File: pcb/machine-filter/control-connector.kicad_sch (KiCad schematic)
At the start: 3 parts

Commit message: Control chips placed; board-to-board connectors found by search: 4 lines (22+3+5+3 pins, 12 ground)
connector_search.py: lines live in legal straight runs on both boards (courtyard polygons, socket body and its
courtyard, leads under bodies), d's ground rules plus a ground on every connector; simulated annealing, 12
restarts. sync_headers.py deletes and re-adds the header footprints from the schematic, places both boards and
checks every pin pair lines up. auto_place.py now keeps other parts' leads out from under a body (U6 had RV4's
lead under it). Mux channels and LED sections re-checked: already shortest. Build OK, raw DRC: no real problems.

Co-Authored-By: Claude Opus 5.5 <noreply@anthropic.com>
Claude-Session: https://claude.ai/code/session_01Cf5qNBi3oNHhbCjPHvswth
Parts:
- added JA4: 1x3 socket, Connector_PinSocket_2.54mm:PinSocket_1x03_P2.54mm_Vertical, symbol Connector_Generic:Conn_01x03
- JA1: value 1x15 socket -> 1x22 socket; footprint Connector_PinSocket_2.54mm:PinSocket_1x15_P2.54mm_Vertical -> Connector_PinSocket_2.54mm:PinSocket_1x22_P2.54mm_Vertical; symbol Connector_Generic:Conn_01x15 -> Connector_Generic:Conn_01x22; MPN 2.54 mm female header 1x15, 8.5 mm (as the Seed3 sockets) -> 2.54 mm female header 1x22, 8.5 mm (as the Seed3 sockets)
- JA2: value 1x13 socket -> 1x3 socket; footprint Connector_PinSocket_2.54mm:PinSocket_1x13_P2.54mm_Vertical -> Connector_PinSocket_2.54mm:PinSocket_1x03_P2.54mm_Vertical; symbol Connector_Generic:Conn_01x13 -> Connector_Generic:Conn_01x03; MPN 2.54 mm female header 1x13, 8.5 mm (as the Seed3 sockets) -> 2.54 mm female header 1x3, 8.5 mm (as the Seed3 sockets)
- JA3: value 1x10 socket -> 1x5 socket; footprint Connector_PinSocket_2.54mm:PinSocket_1x10_P2.54mm_Vertical -> Connector_PinSocket_2.54mm:PinSocket_1x05_P2.54mm_Vertical; symbol Connector_Generic:Conn_01x10 -> Connector_Generic:Conn_01x05; MPN 2.54 mm female header 1x10, 8.5 mm (as the Seed3 sockets) -> 2.54 mm female header 1x5, 8.5 mm (as the Seed3 sockets)
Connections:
- net CTL_+12V: now also JA1.13 (Pin_13); no longer JA1.12 (Pin_12)
- net CTL_+3V3_A: now also JA1.8 (Pin_8); no longer JA3.9 (Pin_9)
- net CTL_-12V: now also JA1.18 (Pin_18); no longer JA1.14 (Pin_14)
- net CTL_CV_BASE: now also JA1.10 (Pin_10); no longer JA2.2 (Pin_2)
- net CTL_CV_DIST: now also JA4.1 (Pin_1); no longer JA2.12 (Pin_12)
- net CTL_CV_EQF: now also JA1.21 (Pin_21); no longer JA2.9 (Pin_9)
- net CTL_CV_EQG: now also JA2.3 (Pin_3); no longer JA2.8 (Pin_8)
- net CTL_CV_HPRES: now also JA1.20 (Pin_20); no longer JA2.5 (Pin_5)
- net CTL_CV_LPRES: now also JA2.1 (Pin_1); no longer JA2.6 (Pin_6)
- net CTL_CV_SRR: now also JA4.3 (Pin_3); no longer JA2.11 (Pin_11)
- net CTL_CV_WIDTH: now also JA1.11 (Pin_11); no longer JA2.3 (Pin_3)
- net CTL_GND: now also JA1.12 (Pin_12), JA1.14 (Pin_14), JA1.17 (Pin_17), JA1.19 (Pin_19), JA1.22 (Pin_22), JA2.2 (Pin_2), JA3.5 (Pin_5), JA4.2 (Pin_2); no longer JA1.11 (Pin_11), JA1.13 (Pin_13), JA1.15 (Pin_15), JA2.1 (Pin_1), JA2.10 (Pin_10), JA2.13 (Pin_13), JA2.4 (Pin_4), JA2.7 (Pin_7), JA3.1 (Pin_1), JA3.10 (Pin_10), JA3.3 (Pin_3), JA3.6 (Pin_6), JA3.8 (Pin_8)
- net CTL_IN_L: now also JA1.6 (Pin_6); no longer JA1.2 (Pin_2)
- net CTL_IN_R: now also JA1.5 (Pin_5); no longer JA1.3 (Pin_3)
- net CTL_LED_A: now also JA3.1 (Pin_1); no longer JA1.10 (Pin_10)
- net CTL_MUX_A: now also JA3.4 (Pin_4); no longer JA3.7 (Pin_7)
- net CTL_MUX_B: now also JA3.2 (Pin_2); no longer JA3.5 (Pin_5)
- net CTL_MUX_C: now also JA3.3 (Pin_3); no longer JA3.4 (Pin_4)
- net CTL_OUT_L: now also JA1.3 (Pin_3); no longer JA1.6 (Pin_6)
- net CTL_OUT_R: now also JA1.2 (Pin_2); no longer JA1.5 (Pin_5)
- net CTL_POT_MUX: now also JA1.16 (Pin_16); no longer JA3.2 (Pin_2)
- net CTL_POT_VOL: now also JA1.15 (Pin_15); no longer JA1.8 (Pin_8)
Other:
- note added: "4 single-row 2.54 mm headers: JA* female on the control board's back, JB* male on the main board's front"
- note added: "JA1: pin 1 at (44.45, 25.4) mm,"
- note added: "JA2: pin 1 at (67.31, 59.69) mm,"
- note added: "JA3: pin 1 at (26.67, 68.58) mm,"
- note added: "JA4: pin 1 at (57.15, 111.76) mm,"
- note removed: "3 single-row 2.54 mm headers: JA* female on the control board's back, JB* male on the main board's front"
- note removed: "JA1: pin 1 at (21.95, 69.205) mm,"
- note removed: "JA2: pin 1 at (41.635, 66.03) mm,"
- note removed: "JA3: pin 1 at (21.95, 84.445) mm,"

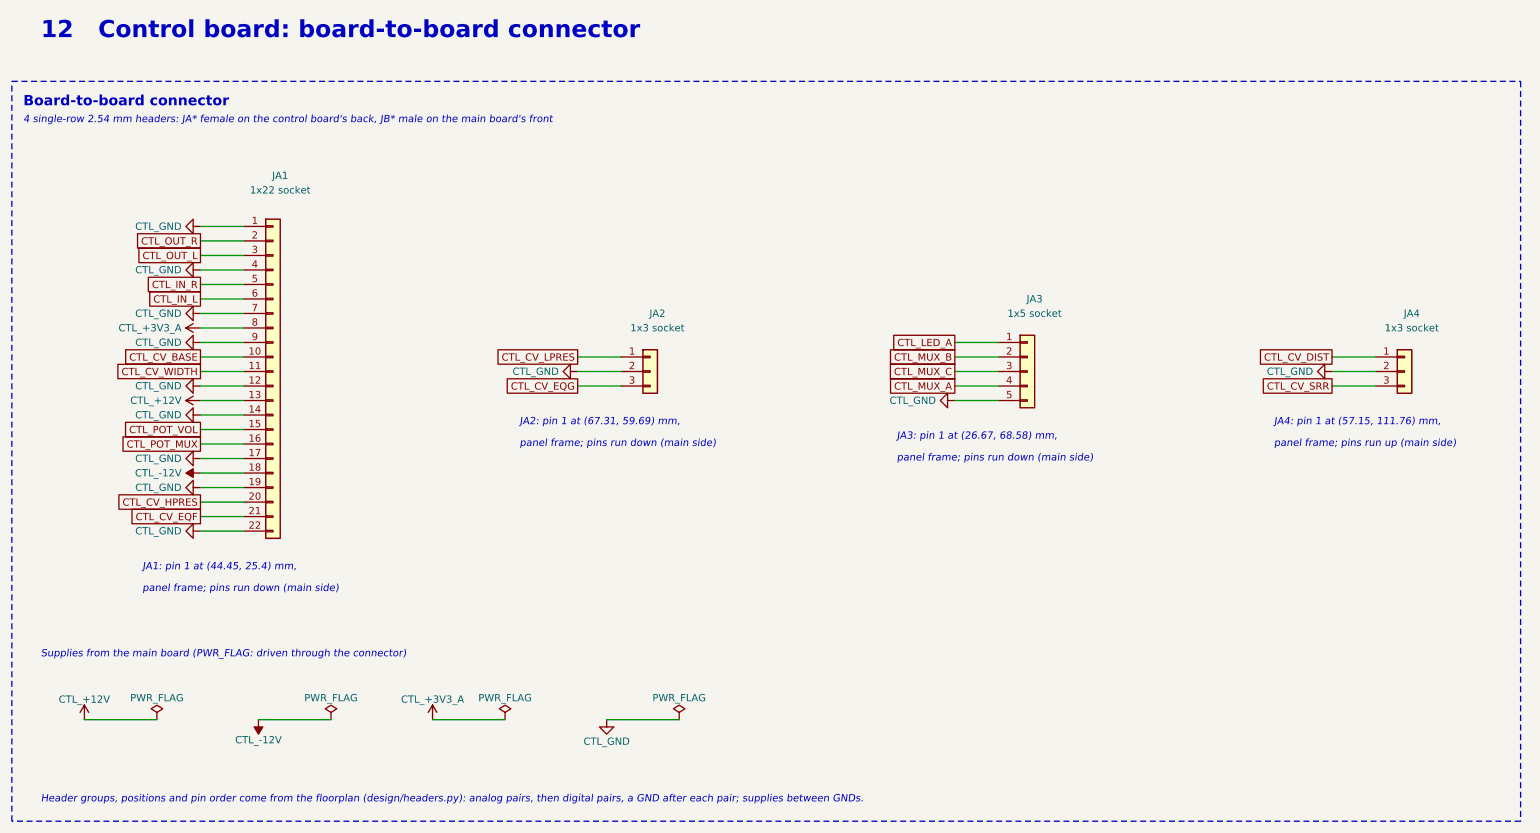
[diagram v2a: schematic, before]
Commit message: Hand-soldering clearance (d: 1.25 mm): connectors re-searched, control parts re-placed
connector_search.py: header pads keep 1.25 mm from every other pad on both boards and from the whole box around
each jack, pot and LED (taken from the square pin-1 pad); --free leaves parts to be re-placed out of the search.
auto_place.py: control-board through-hole pads and anything near a header keep 1.25 mm; --free re-places parts.
Result: 3 lines, 30 + 5 + 2 pins (16 ground); the connector beside pot RV5 and the one between two CV jacks are
gone. Measured: nearest header-pad gap 1.35 mm, header to a body box 1.31 mm. Raw DRC: no real problems.

Co-Authored-By: Claude Opus 5.5 <noreply@anthropic.com>
Claude-Session: https://claude.ai/code/session_01Cf5qNBi3oNHhbCjPHvswth
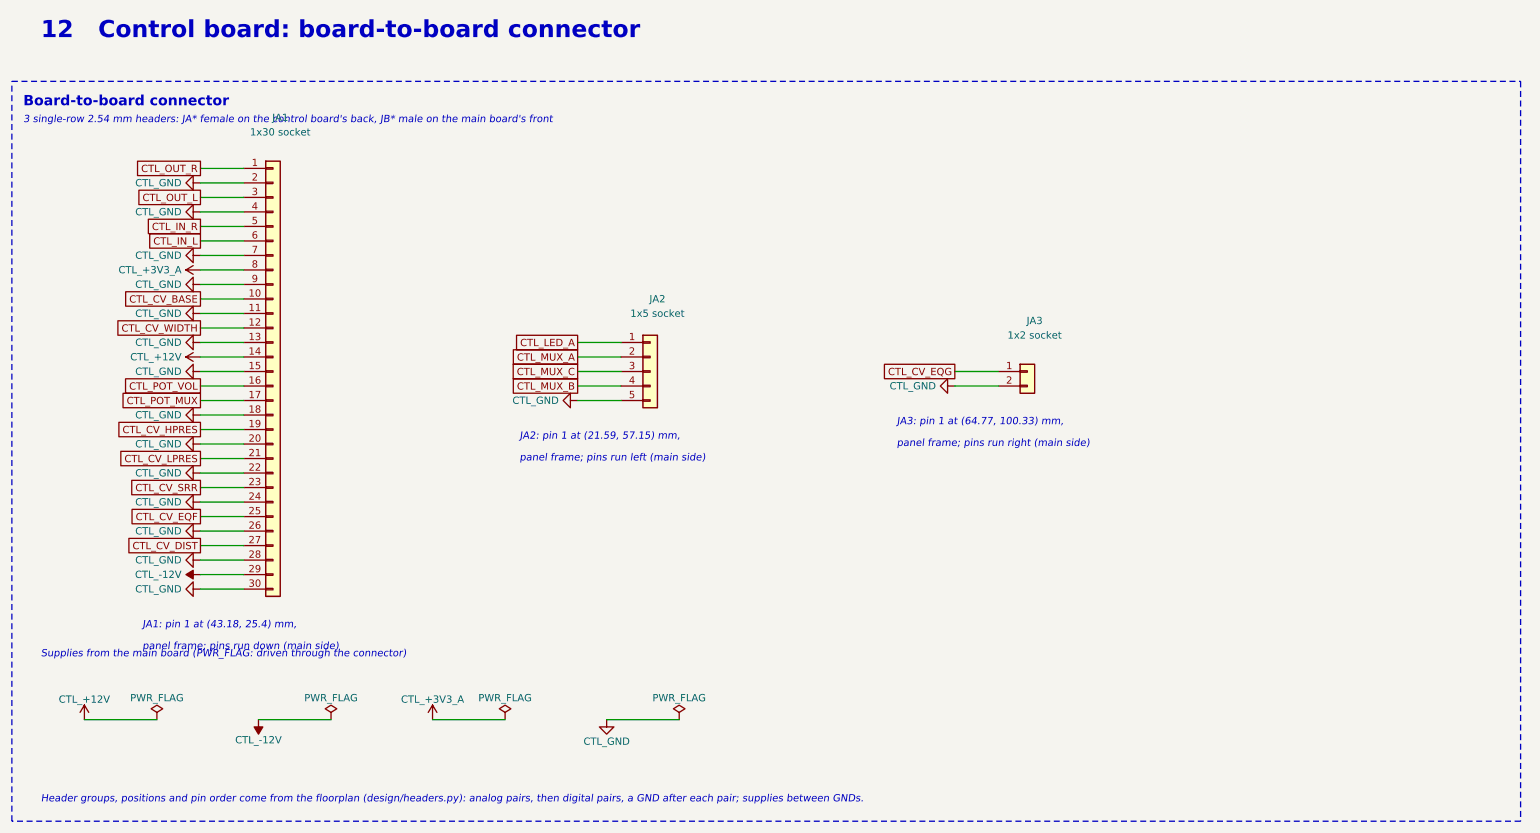
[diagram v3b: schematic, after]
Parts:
- removed JA4: 1x3 socket, Connector_PinSocket_2.54mm:PinSocket_1x03_P2.54mm_Vertical, symbol Connector_Generic:Conn_01x03
- JA1: value 1x22 socket -> 1x30 socket; footprint Connector_PinSocket_2.54mm:PinSocket_1x22_P2.54mm_Vertical -> Connector_PinSocket_2.54mm:PinSocket_1x30_P2.54mm_Vertical; symbol Connector_Generic:Conn_01x22 -> Connector_Generic:Conn_01x30; MPN 2.54 mm female header 1x22, 8.5 mm (as the Seed3 sockets) -> 2.54 mm female header 1x30, 8.5 mm (as the Seed3 sockets)
- JA2: value 1x3 socket -> 1x5 socket; footprint Connector_PinSocket_2.54mm:PinSocket_1x03_P2.54mm_Vertical -> Connector_PinSocket_2.54mm:PinSocket_1x05_P2.54mm_Vertical; symbol Connector_Generic:Conn_01x03 -> Connector_Generic:Conn_01x05; MPN 2.54 mm female header 1x3, 8.5 mm (as the Seed3 sockets) -> 2.54 mm female header 1x5, 8.5 mm (as the Seed3 sockets)
- JA3: value 1x5 socket -> 1x2 socket; footprint Connector_PinSocket_2.54mm:PinSocket_1x05_P2.54mm_Vertical -> Connector_PinSocket_2.54mm:PinSocket_1x02_P2.54mm_Vertical; symbol Connector_Generic:Conn_01x05 -> Connector_Generic:Conn_01x02; MPN 2.54 mm female header 1x5, 8.5 mm (as the Seed3 sockets) -> 2.54 mm female header 1x2, 8.5 mm (as the Seed3 sockets)
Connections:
- net CTL_+12V: now also JA1.14 (Pin_14); no longer JA1.13 (Pin_13)
- net CTL_-12V: now also JA1.29 (Pin_29); no longer JA1.18 (Pin_18)
- net CTL_CV_DIST: now also JA1.27 (Pin_27)
- net CTL_CV_EQF: now also JA1.25 (Pin_25); no longer JA1.21 (Pin_21)
- net CTL_CV_EQG: now also JA3.1 (Pin_1); no longer JA2.3 (Pin_3)
- net CTL_CV_HPRES: now also JA1.19 (Pin_19); no longer JA1.20 (Pin_20)
- net CTL_CV_LPRES: now also JA1.21 (Pin_21); no longer JA2.1 (Pin_1)
- net CTL_CV_SRR: now also JA1.23 (Pin_23)
- net CTL_CV_WIDTH: now also JA1.12 (Pin_12); no longer JA1.11 (Pin_11)
- net CTL_GND: now also JA1.11 (Pin_11), JA1.13 (Pin_13), JA1.15 (Pin_15), JA1.18 (Pin_18), JA1.2 (Pin_2), JA1.20 (Pin_20), JA1.24 (Pin_24), JA1.26 (Pin_26), JA1.28 (Pin_28), JA1.30 (Pin_30), JA2.5 (Pin_5), JA3.2 (Pin_2); no longer JA1.1 (Pin_1), JA1.12 (Pin_12), JA1.14 (Pin_14), JA1.17 (Pin_17), JA1.19 (Pin_19), JA2.2 (Pin_2), JA3.5 (Pin_5)
- net CTL_LED_A: now also JA2.1 (Pin_1); no longer JA3.1 (Pin_1)
- net CTL_MUX_A: now also JA2.2 (Pin_2); no longer JA3.4 (Pin_4)
- net CTL_MUX_B: now also JA2.4 (Pin_4); no longer JA3.2 (Pin_2)
- net CTL_MUX_C: now also JA2.3 (Pin_3); no longer JA3.3 (Pin_3)
- net CTL_OUT_R: now also JA1.1 (Pin_1); no longer JA1.2 (Pin_2)
- net CTL_POT_MUX: now also JA1.17 (Pin_17); no longer JA1.16 (Pin_16)
- net CTL_POT_VOL: now also JA1.16 (Pin_16); no longer JA1.15 (Pin_15)
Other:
- note added: "3 single-row 2.54 mm headers: JA* female on the control board's back, JB* male on the main board's front"
- note added: "JA1: pin 1 at (43.18, 25.4) mm,"
- note added: "JA2: pin 1 at (21.59, 57.15) mm,"
- note added: "JA3: pin 1 at (64.77, 100.33) mm,"
- note added: "panel frame; pins run left (main side)"
- note added: "panel frame; pins run right (main side)"
- note removed: "4 single-row 2.54 mm headers: JA* female on the control board's back, JB* male on the main board's front"
- note removed: "JA1: pin 1 at (44.45, 25.4) mm,"
- note removed: "JA2: pin 1 at (67.31, 59.69) mm,"
- note removed: "JA3: pin 1 at (26.67, 68.58) mm,"
- note removed: "JA4: pin 1 at (57.15, 111.76) mm,"
- note removed: "panel frame; pins run up (main side)"

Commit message: Experiment (not chosen): connectors searched with a strict Seed-pocket rule; routing tool runs
The board now holds the pocket-rule connectors (4 lines, 34 pins) as an experiment; c08-handsolder (3 lines,
routed: main 5 unrouted / 61 vias, control 2 unrouted / 16 vias, DRC 0) stays the best candidate. route_board.py:
Freerouting 2.3 ignores direction costs from DSN, CLI and freerouting.json (tested); 90-degree snap works.
Paused for d: the header loop is repeating (post-mortem 2026-10-06).

Co-Authored-By: Claude Opus 5.5 <noreply@anthropic.com>
Claude-Session: https://claude.ai/code/session_01Cf5qNBi3oNHhbCjPHvswth
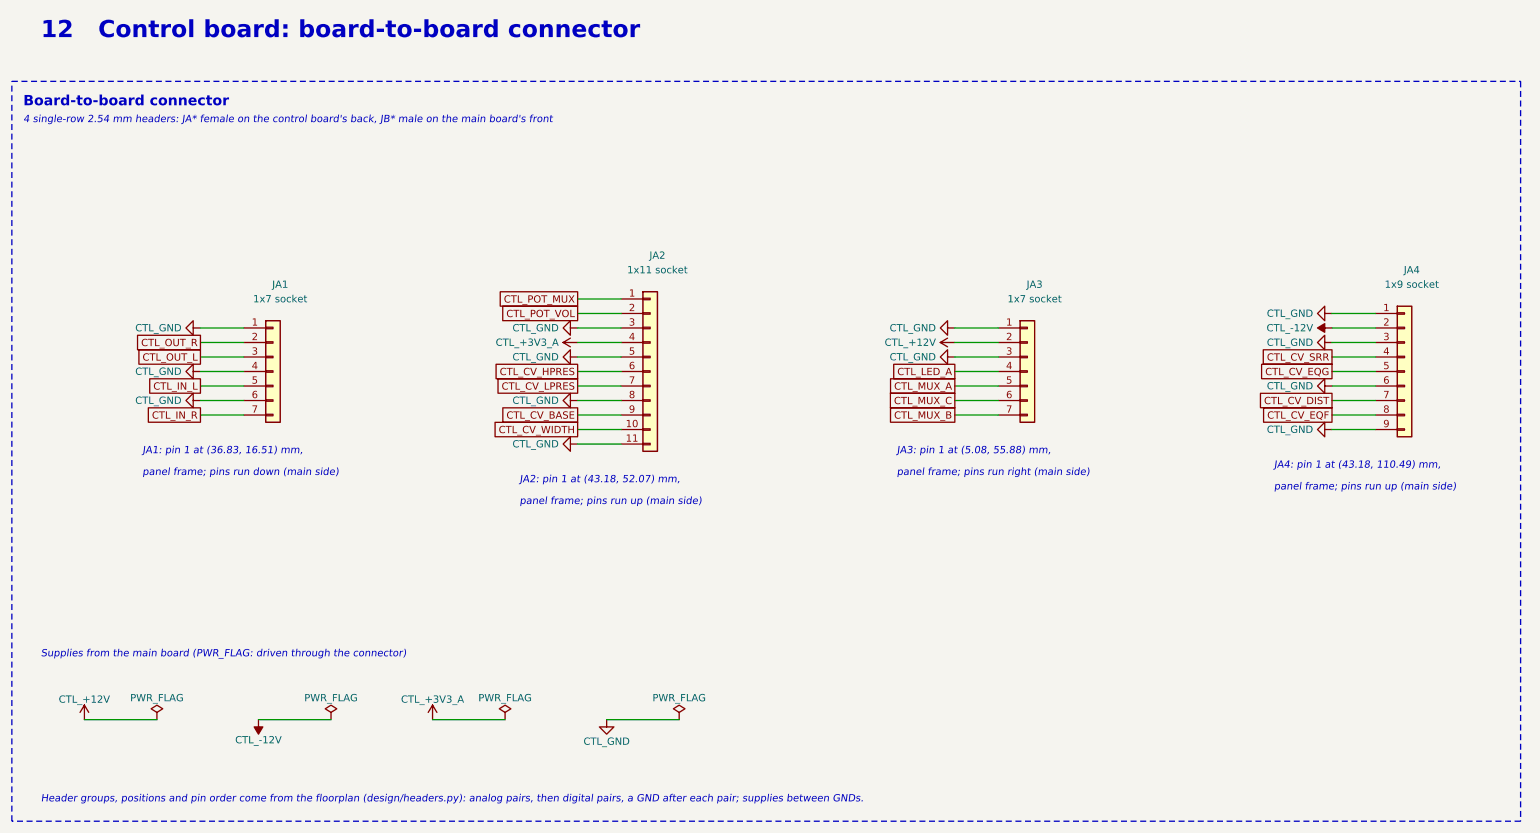
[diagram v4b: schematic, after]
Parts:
- added JA4: 1x9 socket, Connector_PinSocket_2.54mm:PinSocket_1x09_P2.54mm_Vertical, symbol Connector_Generic:Conn_01x09
- JA1: value 1x30 socket -> 1x7 socket; footprint Connector_PinSocket_2.54mm:PinSocket_1x30_P2.54mm_Vertical -> Connector_PinSocket_2.54mm:PinSocket_1x07_P2.54mm_Vertical; symbol Connector_Generic:Conn_01x30 -> Connector_Generic:Conn_01x07; MPN 2.54 mm female header 1x30, 8.5 mm (as the Seed3 sockets) -> 2.54 mm female header 1x7, 8.5 mm (as the Seed3 sockets)
- JA2: value 1x5 socket -> 1x11 socket; footprint Connector_PinSocket_2.54mm:PinSocket_1x05_P2.54mm_Vertical -> Connector_PinSocket_2.54mm:PinSocket_1x11_P2.54mm_Vertical; symbol Connector_Generic:Conn_01x05 -> Connector_Generic:Conn_01x11; MPN 2.54 mm female header 1x5, 8.5 mm (as the Seed3 sockets) -> 2.54 mm female header 1x11, 8.5 mm (as the Seed3 sockets)
- JA3: value 1x2 socket -> 1x7 socket; footprint Connector_PinSocket_2.54mm:PinSocket_1x02_P2.54mm_Vertical -> Connector_PinSocket_2.54mm:PinSocket_1x07_P2.54mm_Vertical; symbol Connector_Generic:Conn_01x02 -> Connector_Generic:Conn_01x07; MPN 2.54 mm female header 1x2, 8.5 mm (as the Seed3 sockets) -> 2.54 mm female header 1x7, 8.5 mm (as the Seed3 sockets)
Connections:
- net CTL_+12V: now also JA3.2 (Pin_2); no longer JA1.14 (Pin_14)
- net CTL_+3V3_A: now also JA2.4 (Pin_4); no longer JA1.8 (Pin_8)
- net CTL_-12V: now also JA4.2 (Pin_2); no longer JA1.29 (Pin_29)
- net CTL_CV_BASE: now also JA2.9 (Pin_9); no longer JA1.10 (Pin_10)
- net CTL_CV_DIST: now also JA4.7 (Pin_7); no longer JA1.27 (Pin_27)
- net CTL_CV_EQF: now also JA4.8 (Pin_8); no longer JA1.25 (Pin_25)
- net CTL_CV_EQG: now also JA4.5 (Pin_5); no longer JA3.1 (Pin_1)
- net CTL_CV_HPRES: now also JA2.6 (Pin_6); no longer JA1.19 (Pin_19)
- net CTL_CV_LPRES: now also JA2.7 (Pin_7); no longer JA1.21 (Pin_21)
- net CTL_CV_SRR: now also JA4.4 (Pin_4); no longer JA1.23 (Pin_23)
- net CTL_CV_WIDTH: now also JA2.10 (Pin_10); no longer JA1.12 (Pin_12)
- net CTL_GND: now also JA1.1 (Pin_1), JA1.6 (Pin_6), JA2.11 (Pin_11), JA2.3 (Pin_3), JA2.8 (Pin_8), JA3.1 (Pin_1), JA3.3 (Pin_3), JA4.1 (Pin_1), JA4.3 (Pin_3), JA4.6 (Pin_6), JA4.9 (Pin_9); no longer JA1.11 (Pin_11), JA1.13 (Pin_13), JA1.15 (Pin_15), JA1.18 (Pin_18), JA1.2 (Pin_2), JA1.20 (Pin_20), JA1.22 (Pin_22), JA1.24 (Pin_24), JA1.26 (Pin_26), JA1.28 (Pin_28), JA1.30 (Pin_30), JA1.7 (Pin_7), JA1.9 (Pin_9), JA3.2 (Pin_2)
- net CTL_IN_L: now also JA1.5 (Pin_5); no longer JA1.6 (Pin_6)
- net CTL_IN_R: now also JA1.7 (Pin_7); no longer JA1.5 (Pin_5)
- net CTL_LED_A: now also JA3.4 (Pin_4); no longer JA2.1 (Pin_1)
- net CTL_MUX_A: now also JA3.5 (Pin_5); no longer JA2.2 (Pin_2)
- net CTL_MUX_B: now also JA3.7 (Pin_7); no longer JA2.4 (Pin_4)
- net CTL_MUX_C: now also JA3.6 (Pin_6); no longer JA2.3 (Pin_3)
- net CTL_OUT_R: now also JA1.2 (Pin_2); no longer JA1.1 (Pin_1)
- net CTL_POT_MUX: now also JA2.1 (Pin_1); no longer JA1.17 (Pin_17)
- net CTL_POT_VOL: now also JA2.2 (Pin_2); no longer JA1.16 (Pin_16)
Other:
- note added: "4 single-row 2.54 mm headers: JA* female on the control board's back, JB* male on the main board's front"
- note added: "JA1: pin 1 at (36.83, 16.51) mm,"
- note added: "JA2: pin 1 at (43.18, 52.07) mm,"
- note added: "JA3: pin 1 at (5.08, 55.88) mm,"
- note added: "JA4: pin 1 at (43.18, 110.49) mm,"
- note added: "panel frame; pins run up (main side)"
- note removed: "3 single-row 2.54 mm headers: JA* female on the control board's back, JB* male on the main board's front"
- note removed: "JA1: pin 1 at (43.18, 25.4) mm,"
- note removed: "JA2: pin 1 at (21.59, 57.15) mm,"
- note removed: "JA3: pin 1 at (64.77, 100.33) mm,"
- note removed: "panel frame; pins run left (main side)"
